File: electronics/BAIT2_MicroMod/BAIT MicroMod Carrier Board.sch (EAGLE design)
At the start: 142 parts, among them J1 SJ-43516-SMT, J10 QWIIC_RIGHT_ANGLE, J15 BM05B-SRSS-TB(LF)(SN), J2 ST-TF-003A, J4 BM05B-SRSS-TB(LF)(SN), J5 QWIIC_RIGHT_ANGLE, J6 JST 2PH, J7 MICROMOD-2222-C, SW1 SKQGADE010, SW2 SKQGADE010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

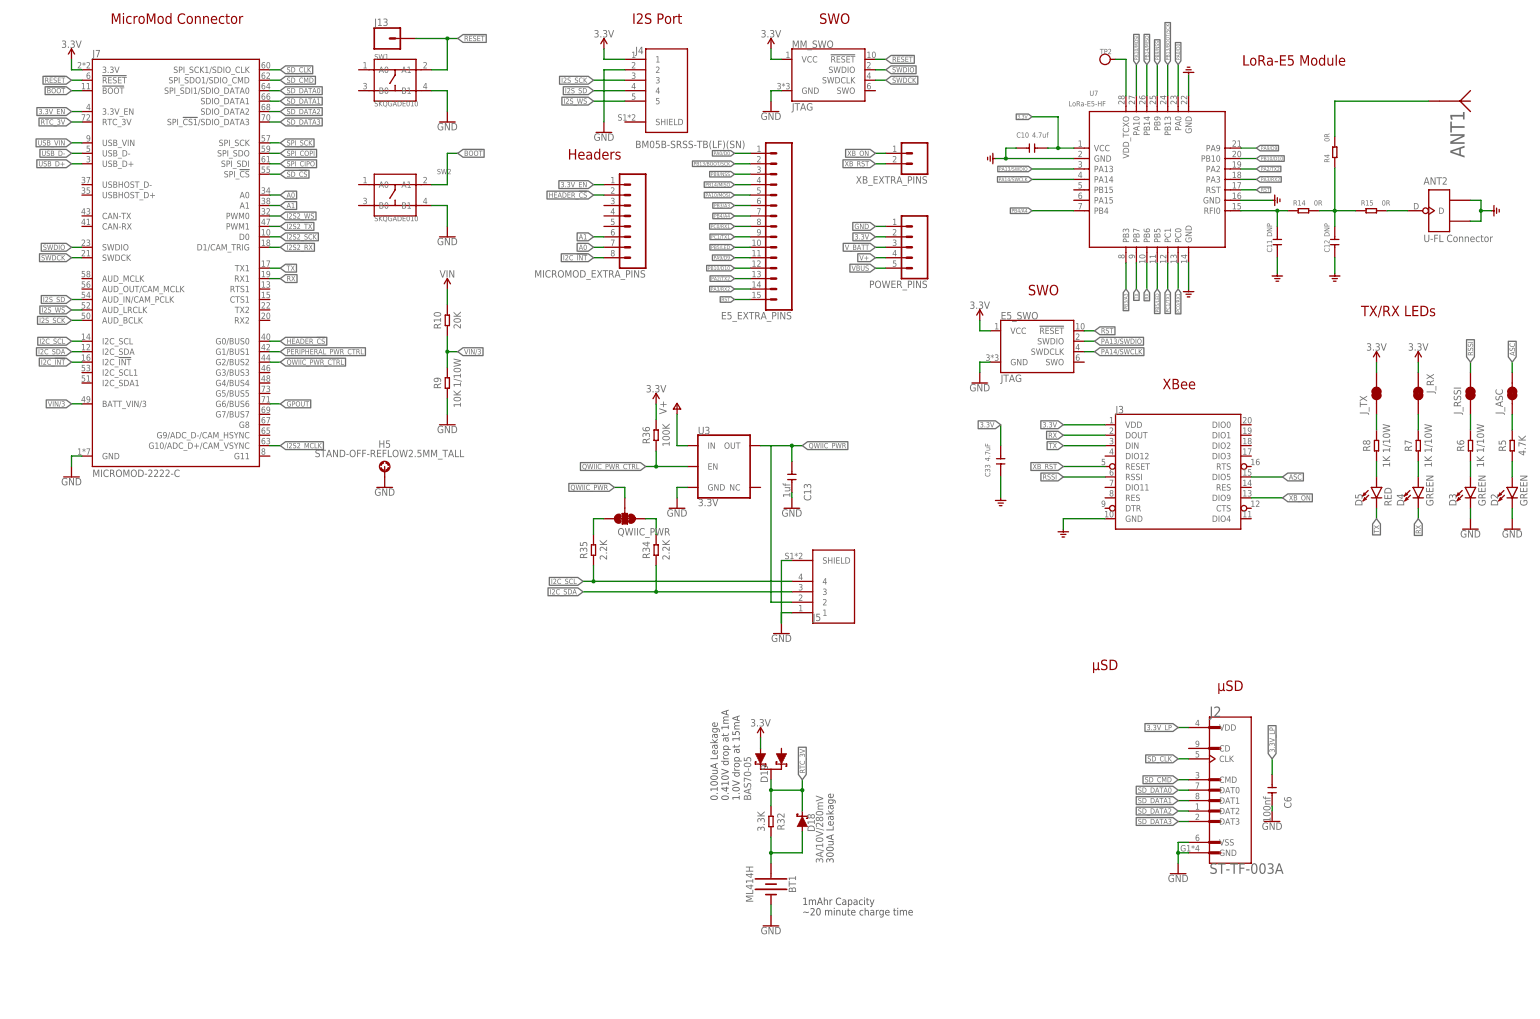
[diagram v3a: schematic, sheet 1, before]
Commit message: Added 3V3 regulators and options to power direct from 3V3 line
Added a regulator for the SGTL5000 and renamed lines from the SD and qwiic regulators. Added enable lines and jumpers to bypass the regulators if necessary.
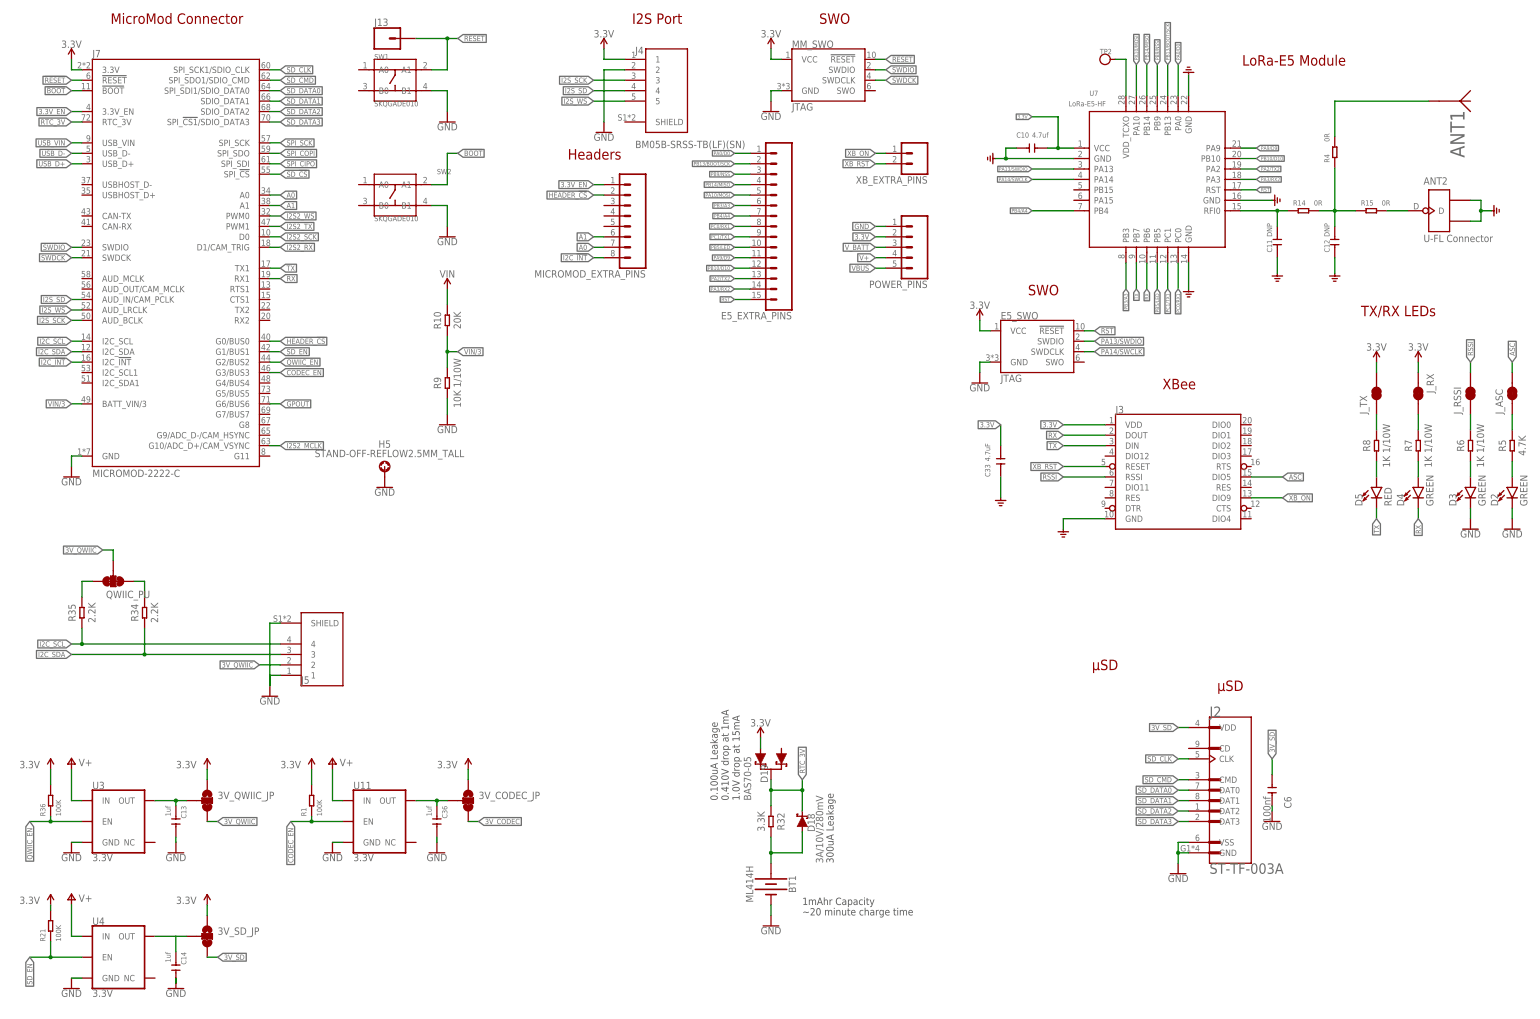
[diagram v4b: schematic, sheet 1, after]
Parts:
- removed QWIIC_PWR: JUMPER-SMT_3_2-NC_TRACE_SILK, SparkFun-Jumpers:JUMPER-SMT_3_2-NC_TRACE_SILK
- added 3V_CODEC_JP, 3V_QWIIC_JP, 3V_SD_JP: MK2_LR, SparkFun-Jumpers:JUMPER-SMT_3_1-NC_TRACE_SILK
- added C36: 1uf, OPL_Capacitor:CERAMIC-1UF-25V-10%-X7R(0603)
- added QWIIC_PU: JUMPER-SMT_3_2-NC_TRACE_SILK, SparkFun-Jumpers:JUMPER-SMT_3_2-NC_TRACE_SILK
- added R1: 100K, OPL_Resistor:SMD-RES-100K-1%-1/10W(0603)
- added U11: 3.3V, SparkFun-IC-Power:V_REG_AP2112K-3.3V
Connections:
- net PERIPHERAL_PWR_CTRL renamed SD_EN
- net QWIIC_PWR_CTRL renamed QWIIC_EN
- removed net 3.3V_LP: C14.1, C6.1, J2.VDD, U4.OUT
- removed net QWIIC_PWR: C13.1, J5.2, QWIIC_PWR.2, U3.OUT
- new net 3V_CODEC: 3V_CODEC_JP.3, C16.+, C17.+, C9.+, FB1.1, U1.VDDIO, U2.IN
- new net 3V_QWIIC: 3V_QWIIC_JP.3, J5.2, QWIIC_PU.2
- new net 3V_QWIIC_OUT: 3V_QWIIC_JP.2, C13.1, U3.OUT
- new net 3V_QWIIC_OUT1: 3V_CODEC_JP.2, C36.1, U11.OUT
- new net 3V_SD: 3V_SD_JP.3, C6.1, J2.VDD
- new net 3V_SD_OUT: 3V_SD_JP.2, C14.1, U4.OUT
- new net CODEC_EN: J7.G3/BUS3, R1.1, U11.EN
- net 3.3V: now also 3V_CODEC_JP.1, 3V_QWIIC_JP.1, 3V_SD_JP.1, R1.2; no longer C16.+, C17.+, C9.+, FB1.1, U1.VDDIO, U2.IN
- net GND: now also C36.2, U11.GND
- net N$24: now also QWIIC_PU.3; no longer QWIIC_PWR.3
- net N$26: now also QWIIC_PU.1; no longer QWIIC_PWR.1
- net V+: now also U11.IN
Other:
- note removed: "Could be a problem that the micromod pinout uses different pins for SDIO than teensy does."
- moved on the sheet: C13, J5, R34, R35, R36, U3

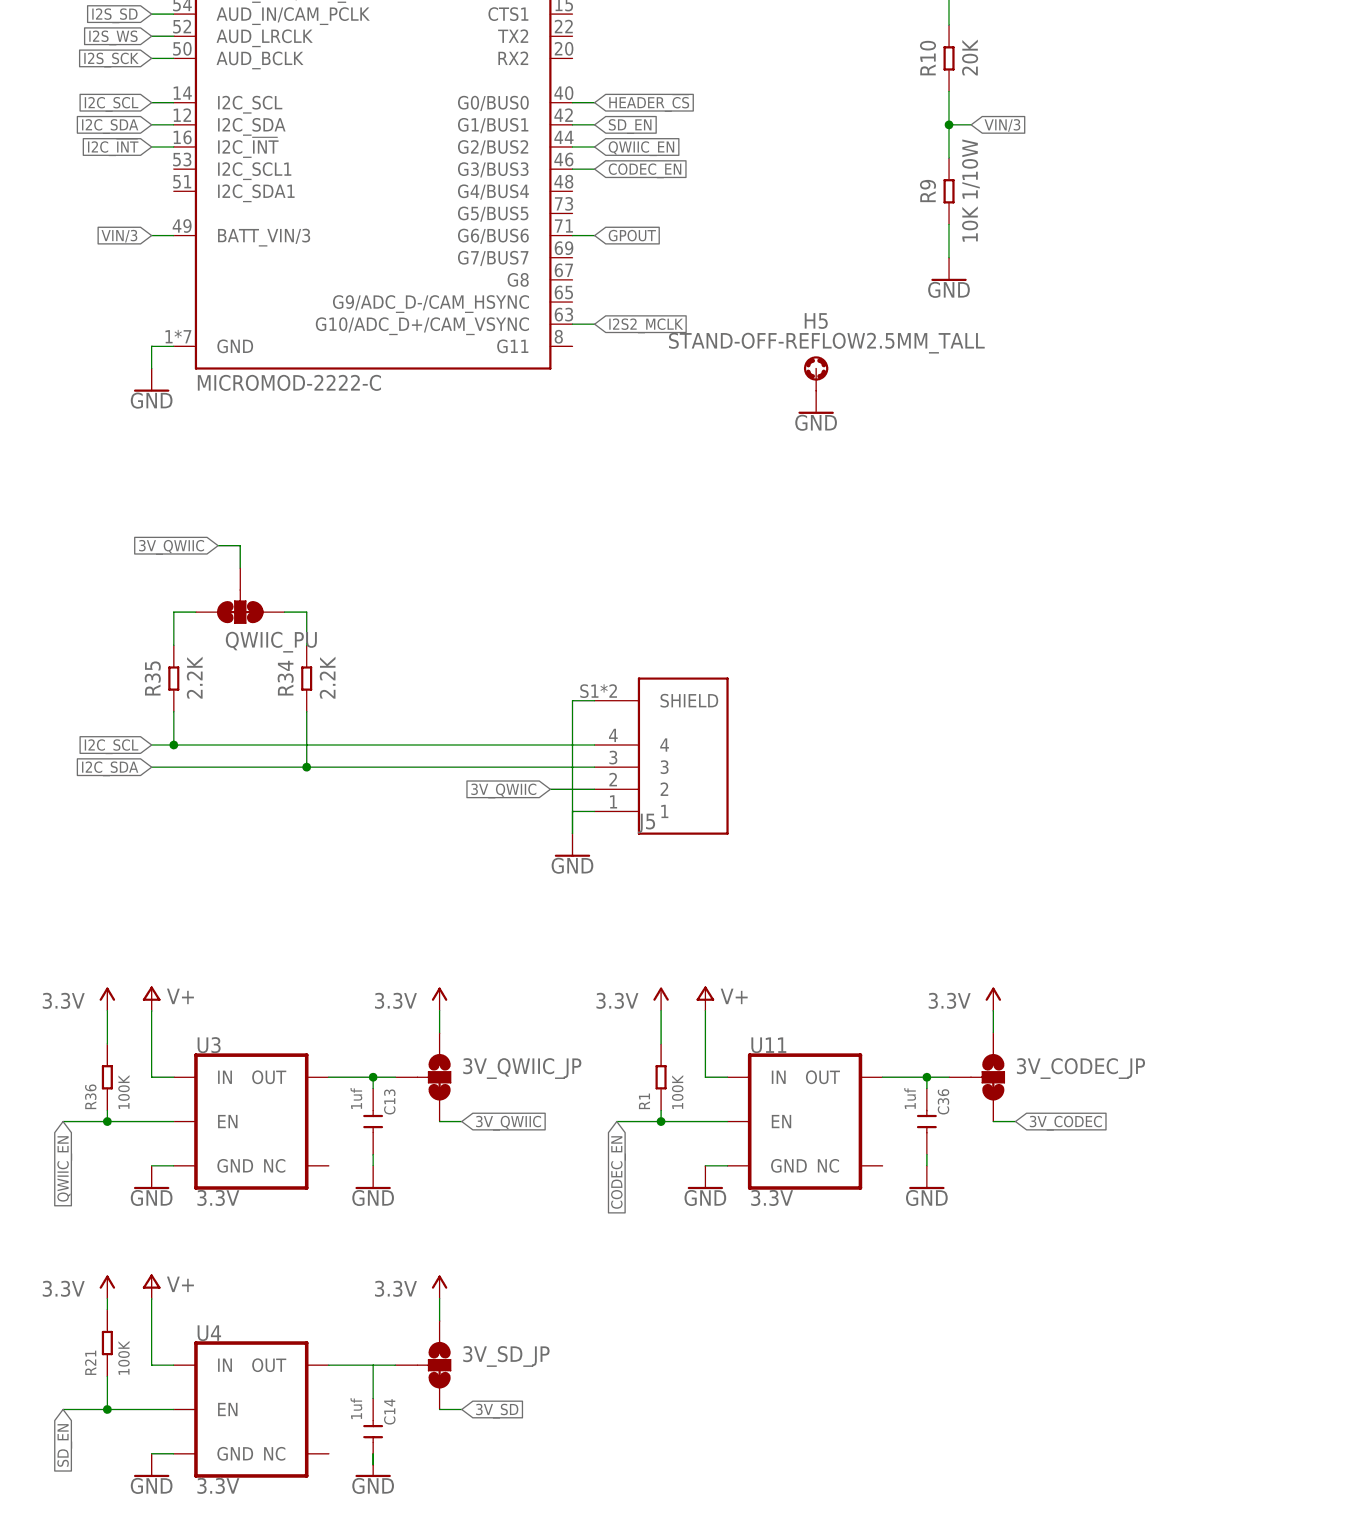
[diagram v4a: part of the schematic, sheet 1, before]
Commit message: Added second Qwiic port, connected to I2C2 (teensy)
Also added power control for this qwiic
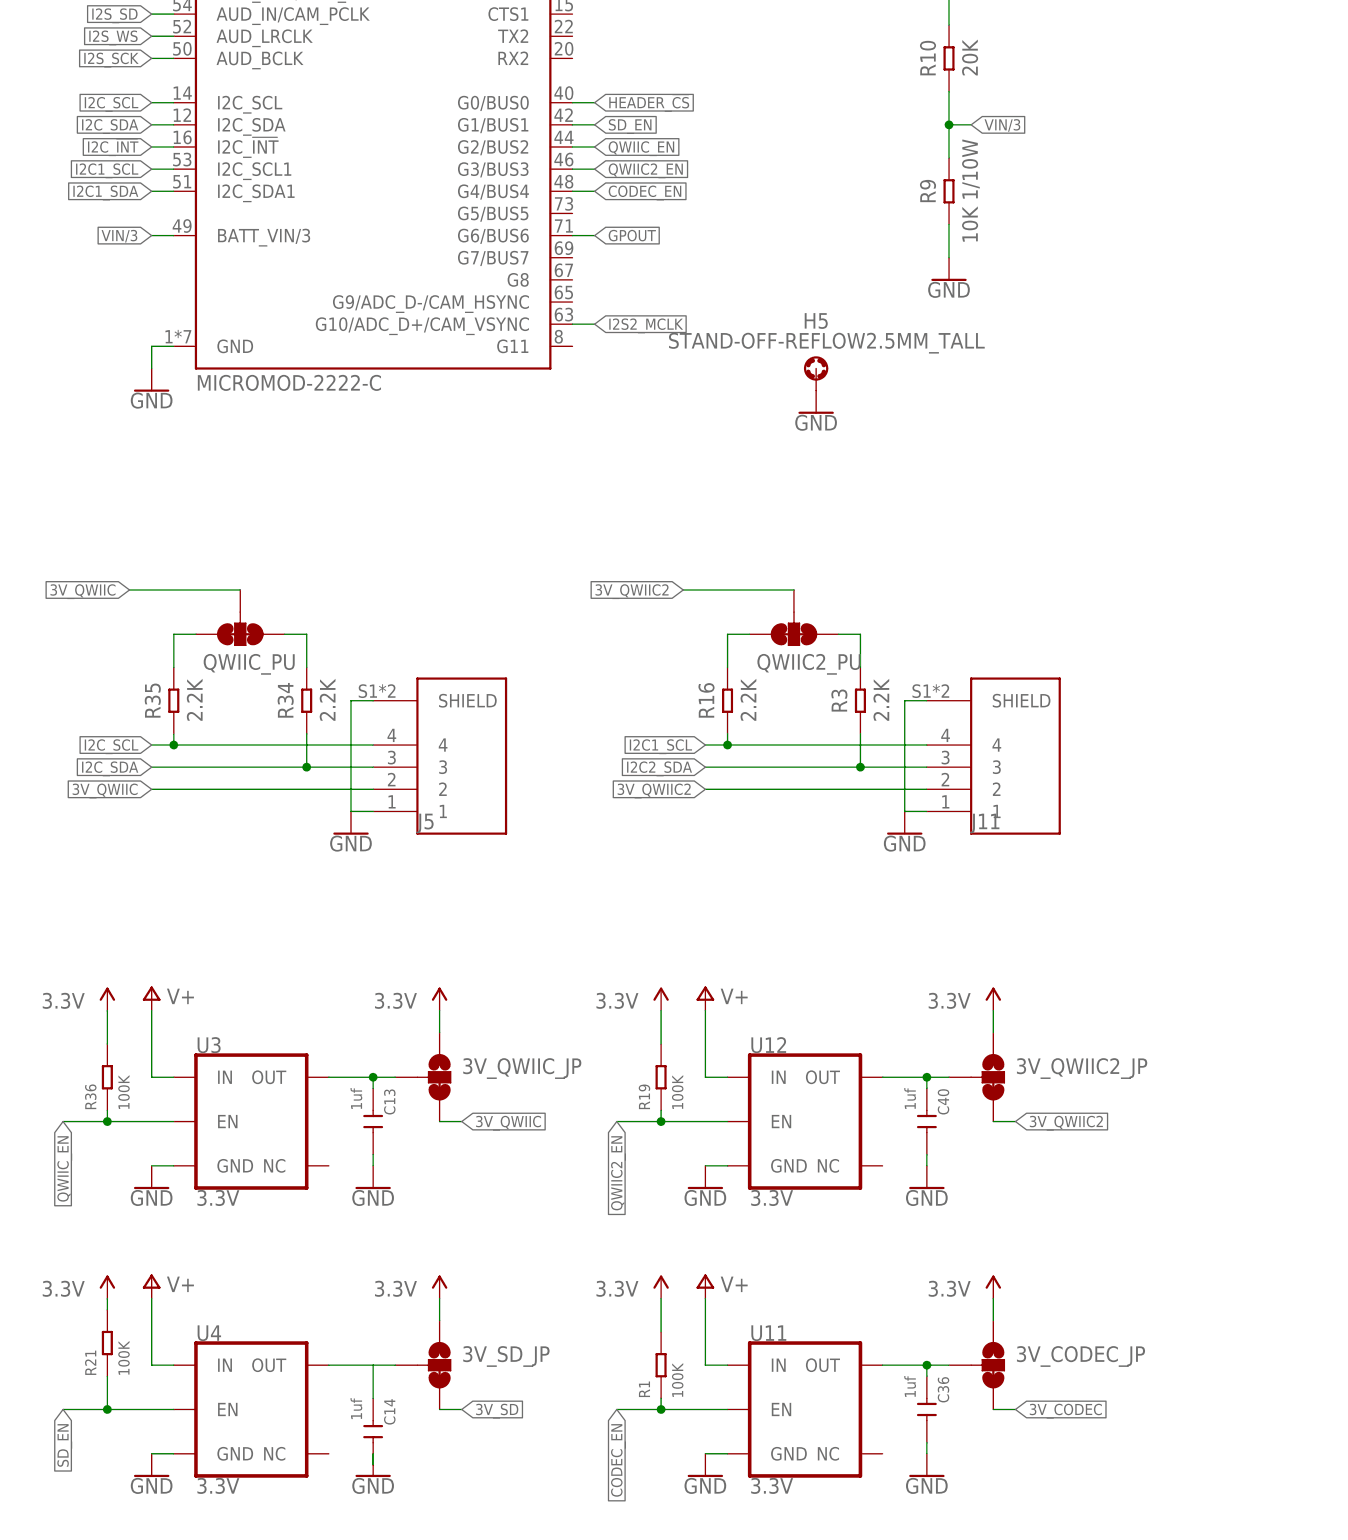
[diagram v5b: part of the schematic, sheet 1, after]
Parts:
- added 3V_QWIIC2_JP: MK2_LR, SparkFun-Jumpers:JUMPER-SMT_3_1-NC_TRACE_SILK
- added C40: 1uf, OPL_Capacitor:CERAMIC-1UF-25V-10%-X7R(0603)
- added J11: QWIIC_RIGHT_ANGLE, JST SH Connectors:BM04B-SRSS-TB(LF)(SN)
- added QWIIC2_PU: JUMPER-SMT_3_2-NC_TRACE_SILK, SparkFun-Jumpers:JUMPER-SMT_3_2-NC_TRACE_SILK
- added R16, R3: 2.2K, OPL_Resistor:SMD-RES-2.2K-5%-1/10W(0603)
- added R19: 100K, OPL_Resistor:SMD-RES-100K-1%-1/10W(0603)
- added U12: 3.3V, SparkFun-IC-Power:V_REG_AP2112K-3.3V
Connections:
- new net 3V_QWIIC2: 3V_QWIIC2_JP.3, J11.2, QWIIC2_PU.2
- new net 3V_QWIIC_OUT2: 3V_QWIIC2_JP.2, C40.1, U12.OUT
- new net I2C1_SCL: J11.4, J7.I2C_SCL1, R16.1
- new net I2C1_SDA: J7.I2C_SDA1
- new net I2C2_SDA: J11.3, R3.1
- new net N$1: QWIIC2_PU.3, R16.2
- new net N$2: QWIIC2_PU.1, R3.2
- new net QWIIC2_EN: J7.G3/BUS3, R19.1, U12.EN
- net 3.3V: now also 3V_QWIIC2_JP.1, R19.2
- net CODEC_EN: now also J7.G4/BUS4; no longer J7.G3/BUS3
- net GND: now also C40.2, J11.1, J11.SHIELD, U12.GND
- net V+: now also U12.IN
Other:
- moved on the sheet: 3V_CODEC_JP, C36, J5, QWIIC_PU, R1, R34, R35, U11
